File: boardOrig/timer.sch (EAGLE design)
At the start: 46 parts, among them IC1 7805T, IC6 DS1307, U1 ATMEGA328P

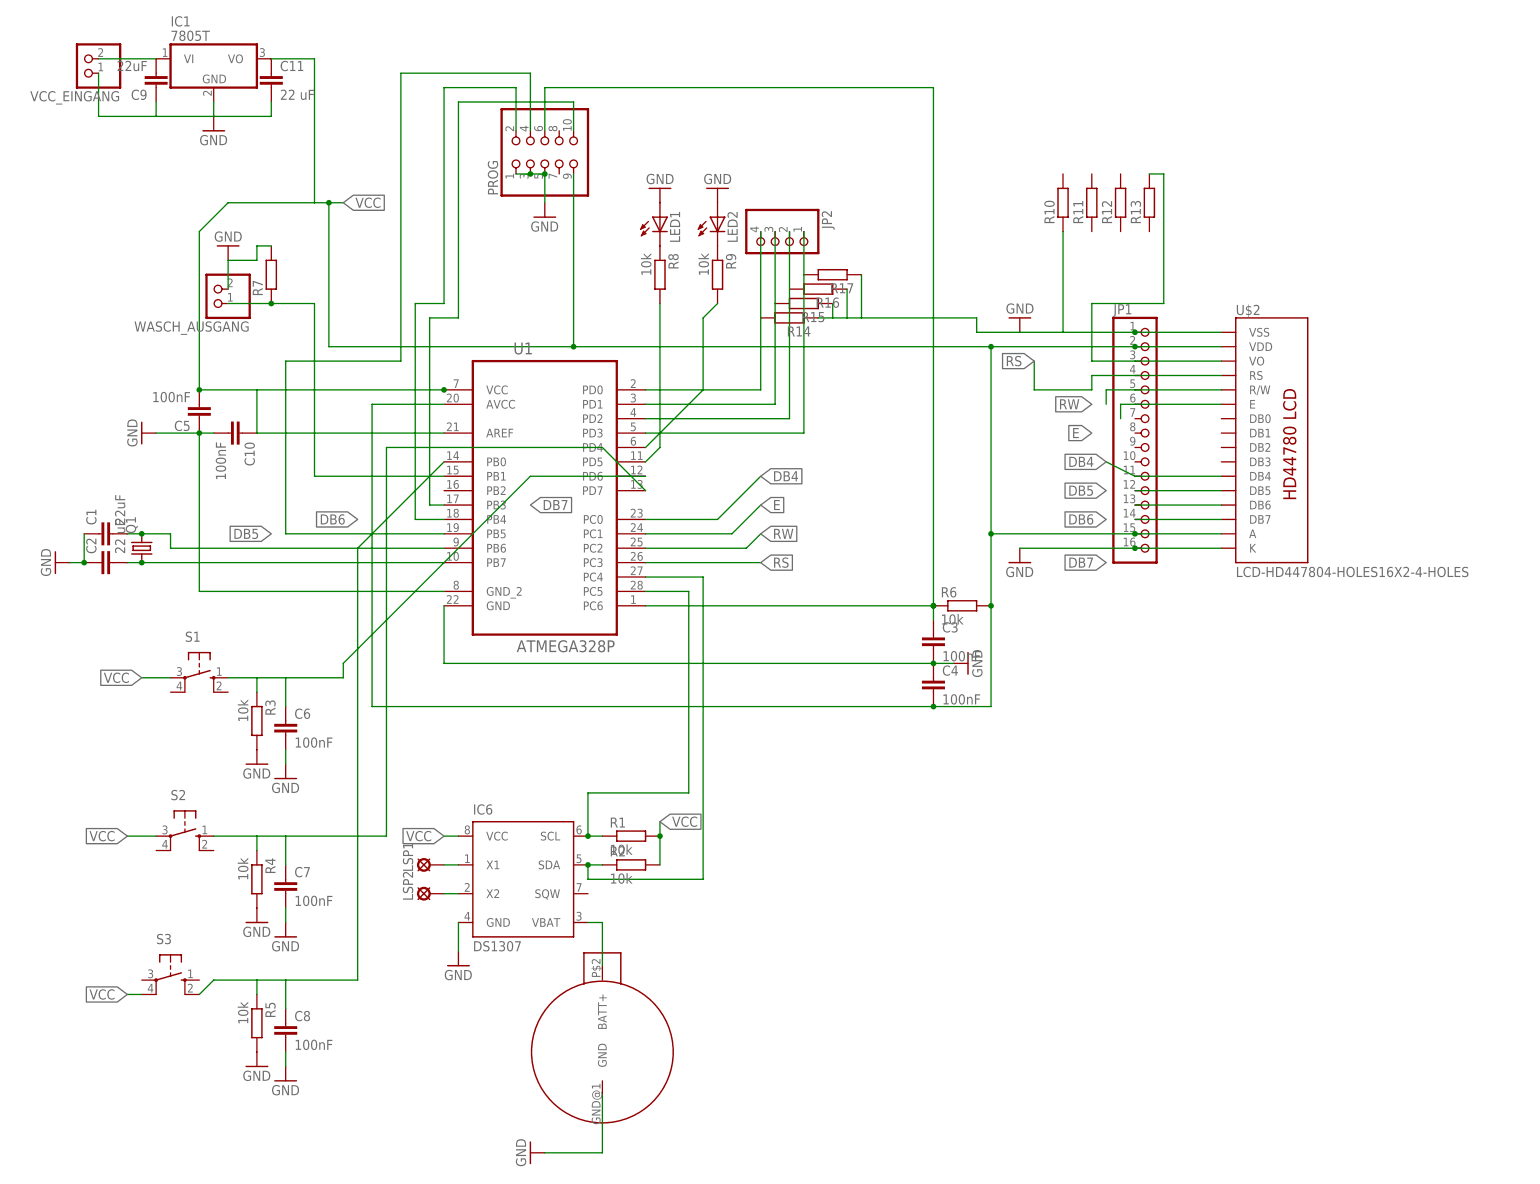
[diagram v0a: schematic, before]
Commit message: Updated Board and added DS1307 to Program
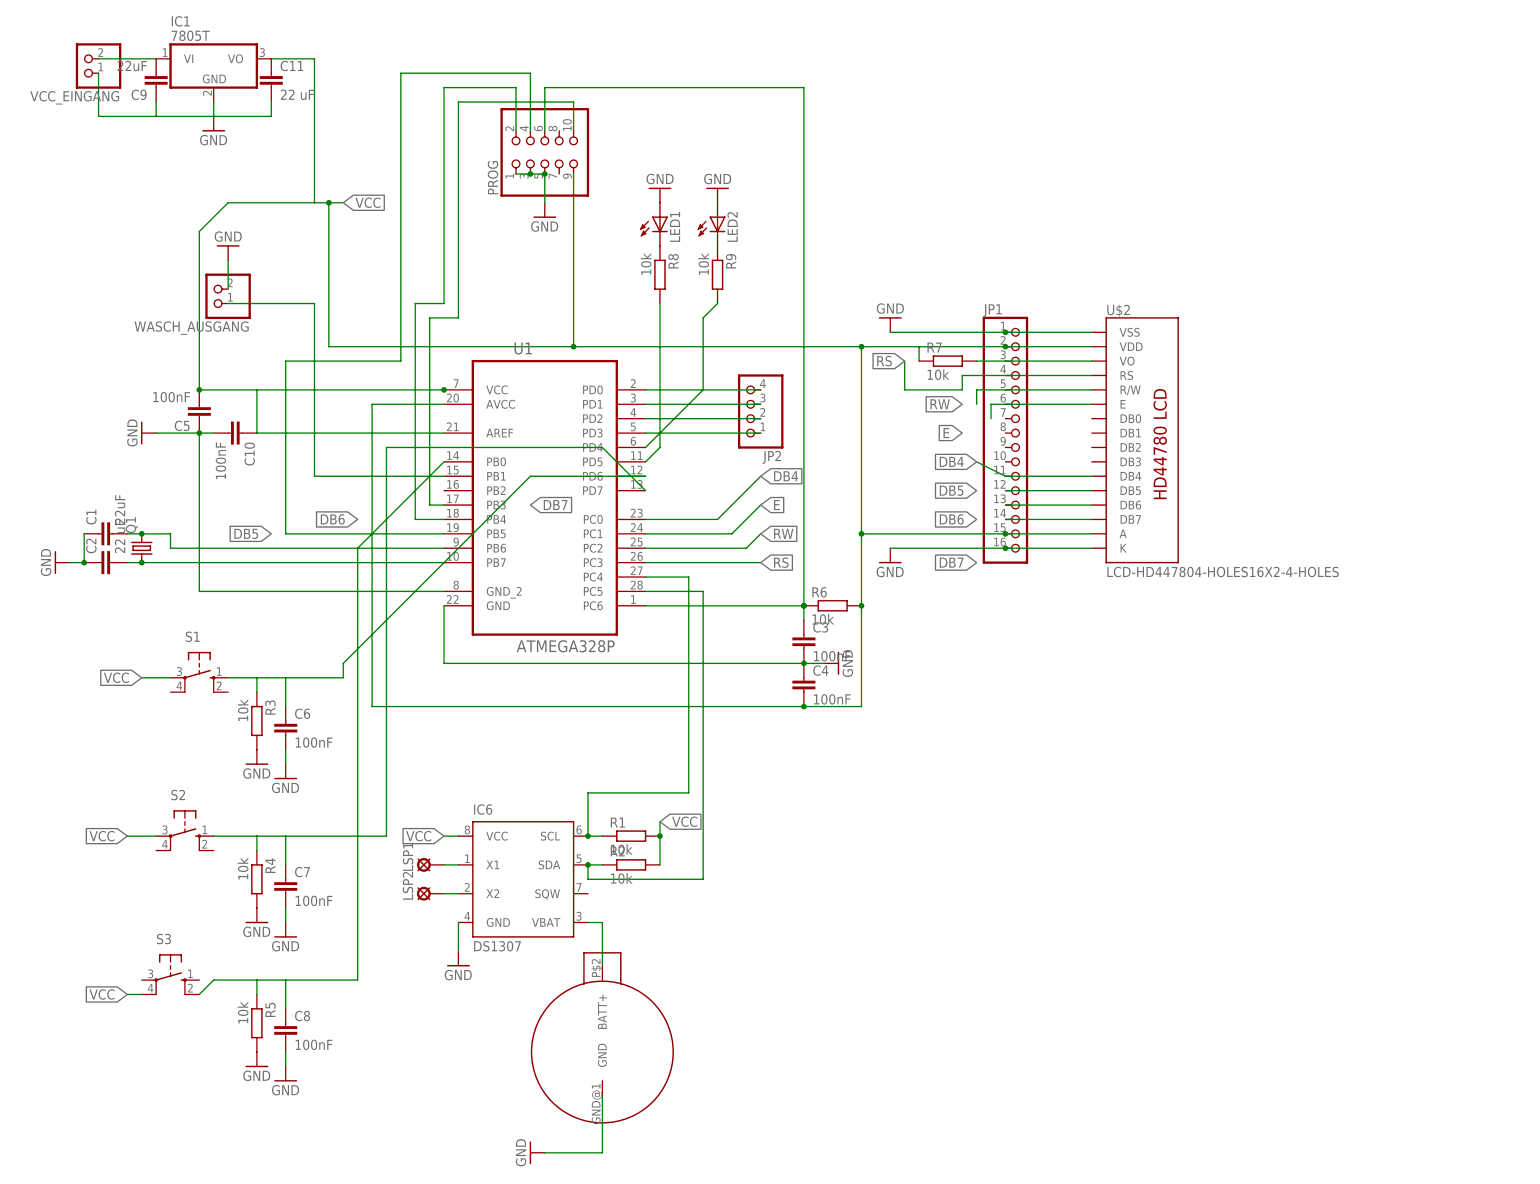
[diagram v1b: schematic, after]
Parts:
- removed R10, R11, R12, R13, R14, R15, R16, R17: (no value), eagle-ltspice:RR0603
- R7: value (none) -> 10k; device eagle-ltspice:RR0603 -> resistor:R-EU_0204/7
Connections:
- removed net N$15: JP2.4, R14.2, U1.PD0
- removed net N$17: JP2.2, R16.2, U1.PD2
- new net N$10: JP2.2, U1.PD2
- new net N$6: JP2.4, U1.PD0
- net GND: no longer R10.1, R14.1, R15.1, R16.1, R17.1, R7.2
- net N$12: no longer R17.2
- net N$2: now also R7.2; no longer R13.2
- net N$3: no longer R7.1
- net N$39: now also U1.PC4; no longer U1.PC5
- net N$40: now also U1.PC5; no longer U1.PC4
- net N$9: no longer R15.2
- net VCC: now also R7.1
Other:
- moved on the sheet: C3, C4, JP1, JP2, R6, R7, U$2
